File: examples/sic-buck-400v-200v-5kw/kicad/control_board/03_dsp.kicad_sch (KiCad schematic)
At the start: 1 part, among them U5 TMS320F28335PGFA

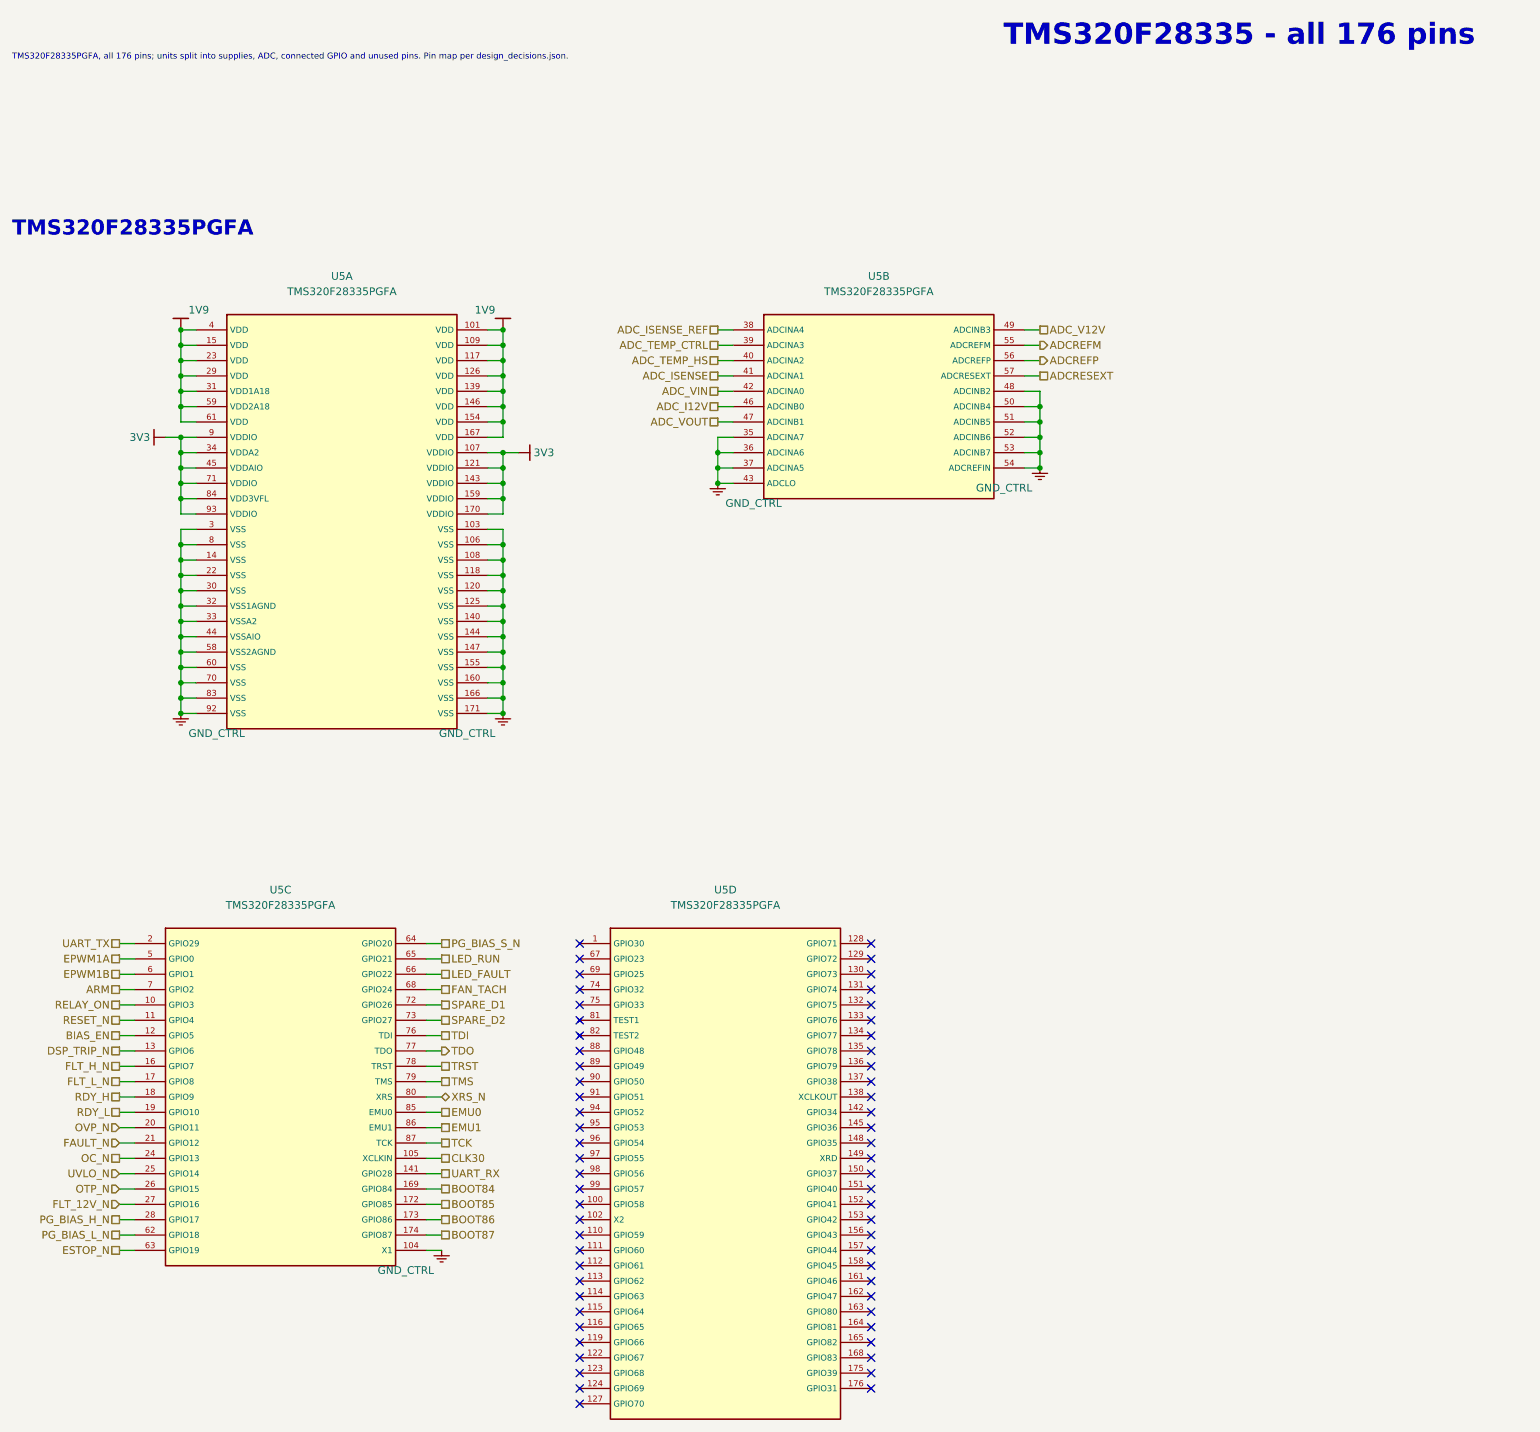
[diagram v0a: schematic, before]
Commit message: Correct sensing circuits and add verified V2.2 local bypasses
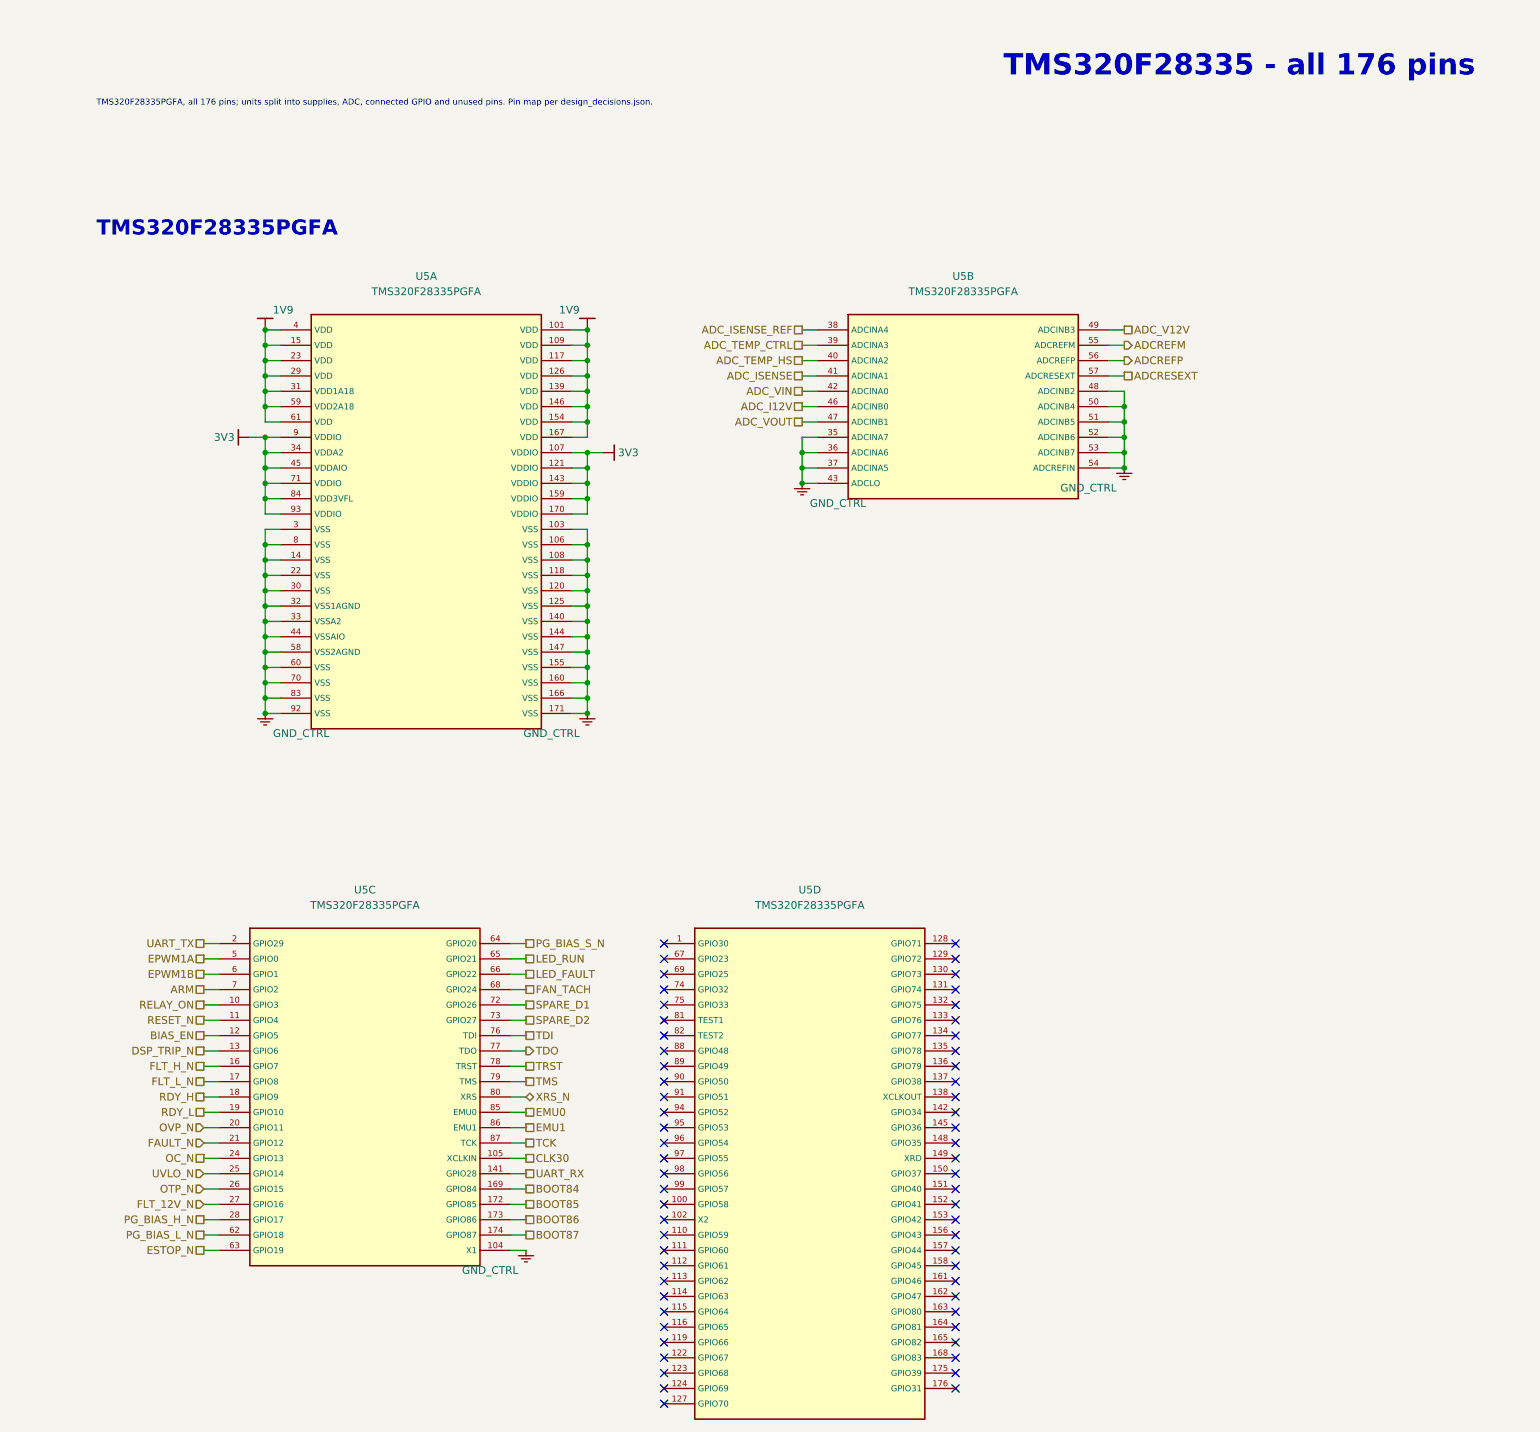
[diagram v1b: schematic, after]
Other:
- moved on the sheet: U5A, U5B, U5C, U5D
